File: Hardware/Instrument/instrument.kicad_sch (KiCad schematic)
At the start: 0 parts

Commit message: Added untested op amp circuits for all three devices.
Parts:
- added C3: 1uF, symbol Device:C_Small
- added J1, J3: Esp32 socket, Connector_PinSocket_2.54mm:PinSocket_1x19_P2.54mm_Vertical, symbol Connector:Conn_01x19_Socket
- added MK1: Electret microphone, symbol Device:Microphone
- added R2: 1.5k?, symbol Device:R_Small
- added R7: 100k?, symbol Device:R_Small
- added R8: 500k, symbol Device:R_Small
- added R9: 500k?, symbol Device:R_Small
- added RV2: 1M?, symbol Device:R_Potentiometer_Trim
- added U2: MCP6002-xP, symbol Amplifier_Operational:MCP6002-xP
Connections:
- new net: R8.2, R9.1, U2.3 (+)
- new net: R7.2, RV2.2, RV2.3, U2.2 (-)
- new net: C3.1, MK1.2 (+), R2.2
- new net: C3.2, R7.1
- new net: U2.5 (+), U2.6 (-)
- new net +3.3V: J3.1 (Pin_1), R2.1, R9.2, U2.8 (V+)
- new net +5V: J3.19 (Pin_19)
- new net 0: J1.14 (Pin_14)
- new net 12: J3.13 (Pin_13)
- new net 13: J3.15 (Pin_15)
- new net 14: J3.12 (Pin_12)
- new net 15: J1.16 (Pin_16)
- new net 16: J1.12 (Pin_12)
- new net 17: J1.11 (Pin_11)
- new net 18: J1.9 (Pin_9)
- new net 19: J1.8 (Pin_8)
- new net 2: J1.15 (Pin_15)
- new net 21: J1.6 (Pin_6)
- new net 22: J1.3 (Pin_3)
- new net 23: J1.2 (Pin_2)
- new net 26: J3.10 (Pin_10)
- new net 27: J3.11 (Pin_11)
- new net 32: J3.7 (Pin_7)
- new net 33: J3.8 (Pin_8)
- new net 34: J3.5 (Pin_5)
- new net 35: J3.6 (Pin_6)
- new net 4: J1.13 (Pin_13)
- new net 5: J1.10 (Pin_10)
- new net CLK: J1.19 (Pin_19)
- new net CMD: J3.18 (Pin_18)
- new net D1: J1.17 (Pin_17)
- new net D2: J3.16 (Pin_16)
- new net D3: J3.17 (Pin_17)
- new net D9: J1.18 (Pin_18)
- new net DAC1: J3.9 (Pin_9)
- new net EN: J3.2 (Pin_2)
- new net GND: J1.1 (Pin_1), J1.7 (Pin_7), J3.14 (Pin_14), MK1.1 (-), R8.1, U2.4 (V-)
- new net RX: J1.5 (Pin_5)
- new net TX: J1.4 (Pin_4)
- new net VN: J3.4 (Pin_4)
- new net VP: J3.3 (Pin_3), RV2.1, U2.1
- no-connect marks 0 -> 1
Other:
- note added: "ESP32"

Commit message: added PDF of hardware. Very small (if any) hardware changes.
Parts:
- R7: value 100k? -> 50k?
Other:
- note added: "LP filter?"
- note added: "MULTICOMP PRO ABM-713-RC"
- moved on the sheet: C3, MK1, R2, R7, R8, R9, RV2, U2A

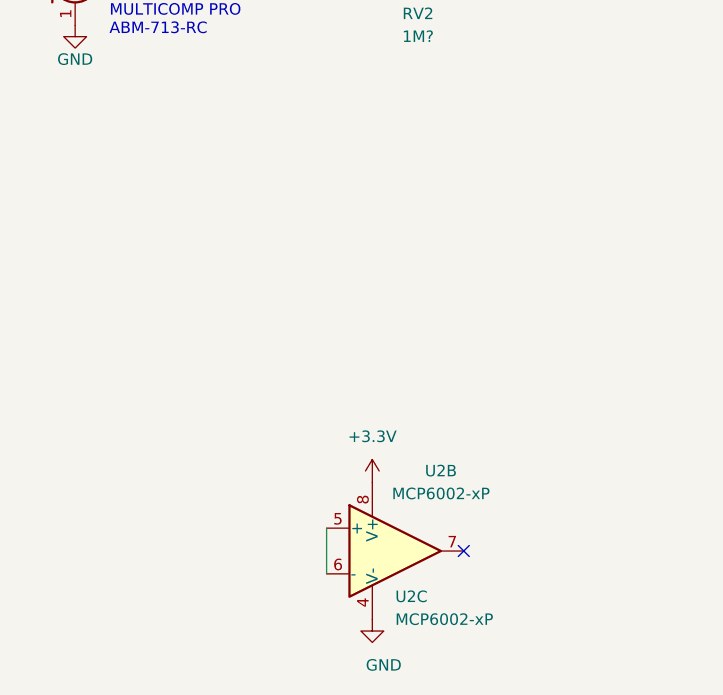
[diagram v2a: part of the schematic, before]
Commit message: Greatly simplified the gateway/speaker module. Added a rectifying circuit and a comparator circuit to the bass drum module. Solidified some component values. Added decoupling capacitors to the schematic.
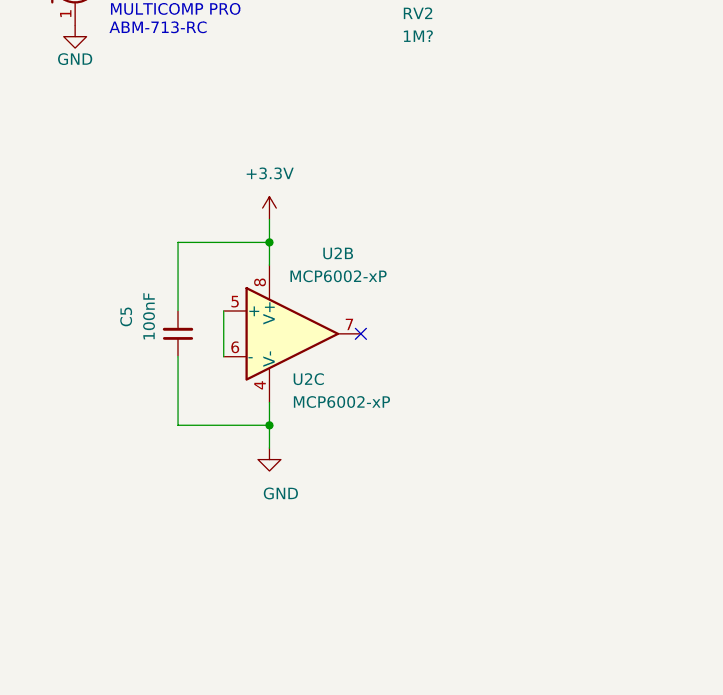
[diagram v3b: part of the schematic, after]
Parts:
- added C5: 100nF, symbol Device:C_Small
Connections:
- net +3.3V: now also C5.2
- net GND: now also C5.1
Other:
- moved on the sheet: U2B, U2C
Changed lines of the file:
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@@
     (company "Studentorchesteret den Ohmske Motstanden")
   )
+  (junction (at 53.34 147.32) (diameter 0) (color 0 0 0 0)
+  )
   (junction (at 80.01 87.63) (diameter 0) (color 0 0 0 0)
   )
@@
   (junction (at 62.23 90.17) (diameter 0) (color 0 0 0 0)
   )
+  (junction (at 53.34 127) (diameter 0) (color 0 0 0 0)
+  )
   (junction (at 62.23 95.25) (diameter 0) (color 0 0 0 0)
   )
-  (no_connect (at 74.93 161.29))
+  (no_connect (at 63.5 137.16))
   (wire (pts (xy 59.69 90.17) (xy 62.23 90.17))
     (stroke (width 0) (type default))
@@
     (stroke (width 0) (type default))
   )
+  (wire (pts (xy 53.34 149.86) (xy 53.34 147.32))
+    (stroke (width 0) (type default))
+  )
   (wire (pts (xy 55.88 66.04) (xy 55.88 68.58))
     (stroke (width 0) (type default))
   )
+  (wire (pts (xy 53.34 124.46) (xy 53.34 127))
+    (stroke (width 0) (type default))
+  )
   (wire (pts (xy 133.35 115.57) (xy 128.27 115.57))
     (stroke (width 0) (type default))
   )
+  (wire (pts (xy 53.34 127) (xy 43.18 127))
+    (stroke (width 0) (type default))
+  )
   (wire (pts (xy 34.29 90.17) (xy 31.75 90.17))
     (stroke (width 0) (type default))
@@
     (stroke (width 0) (type default))
   )
+  (wire (pts (xy 53.34 127) (xy 53.34 129.54))
+    (stroke (width 0) (type default))
+  )
   (wire (pts (xy 31.75 90.17) (xy 31.75 92.71))
     (stroke (width 0) (type default))
@@
     (stroke (width 0) (type default))
   )
+  (wire (pts (xy 53.34 147.32) (xy 53.34 144.78))
+    (stroke (width 0) (type default))
+  )
   (wire (pts (xy 69.85 99.06) (xy 62.23 99.06))
     (stroke (width 0) (type default))
   )
+  (wire (pts (xy 43.18 127) (xy 43.18 134.62))
+    (stroke (width 0) (type default))
+  )
   (wire (pts (xy 55.88 68.58) (xy 62.23 68.58))
     (stroke (width 0) (type default))
@@
     (stroke (width 0) (type default))
   )
-  (wire (pts (xy 59.69 158.75) (xy 59.69 163.83))
+  (wire (pts (xy 48.26 134.62) (xy 48.26 139.7))
     (stroke (width 0) (type default))
   )
@@
     (stroke (width 0) (type default))
   )
+  (wire (pts (xy 43.18 147.32) (xy 53.34 147.32))
+    (stroke (width 0) (type default))
+  )
   (wire (pts (xy 80.01 95.25) (xy 80.01 87.63))
     (stroke (width 0) (type default))
@@
     (stroke (width 0) (type default))
   )
+  (wire (pts (xy 43.18 139.7) (xy 43.18 147.32))
+    (stroke (width 0) (type default))
+  )
   (rectangle (start 170.18 133.35) (end 107.95 71.12)
     (stroke (width 0) (type default))
@@
     (effects (font (size 1.27 1.27)) (justify left bottom))
   )
+  (symbol (lib_id "Device:C_Small") (at 43.18 137.16 180) (unit 1)
+    (in_bom yes) (on_board yes) (dnp no)
+    (property "Reference" "C5" (at 37.465 135.255 90)
+      (effects (font (size 1.27 1.27)))
+    )
+    (property "Value" "100nF" (at 40.005 135.255 90)
+      (effects (font (size 1.27 1.27)))
+    )
+    (property "Footprint" "" (at 43.18 137.16 0)
+      (effects (font (size 1.27 1.27)) hide)
+    )
+    (property "Datasheet" "~" (at 43.18 137.16 0)
+      (effects (font (size 1.27 1.27)) hide)
+    )
+    (pin "1")
+    (pin "2")
+    (instances
+      (project "Stink-overview"
+        (path "/cabf8207-5290-464d-a5db-d31c713ce03c/9cff79f6-1e38-4fd8-974e-e06f4e0c362c"
+          (reference "C5") (unit 1)
+        )
+      )
+    )
+  )
   (symbol (lib_id "power:PWR_FLAG") (at 137.16 82.55 270) (unit 1)
     (in_bom yes) (on_board yes) (dnp no)
@@
     )
   )
-  (symbol (lib_id "power:+3.3V") (at 64.77 153.67 0) (unit 1)
+  (symbol (lib_id "power:+3.3V") (at 53.34 124.46 0) (unit 1)
     (in_bom yes) (on_board yes) (dnp no) (fields_autoplaced)
-    (property "Reference" "#PWR03" (at 64.77 157.48 0)
+    (property "Reference" "#PWR03" (at 53.34 128.27 0)
       (effects (font (size 1.27 1.27)) hide)
     )
-    (property "Value" "+3.3V" (at 64.77 148.59 0)
+    (property "Value" "+3.3V" (at 53.34 119.38 0)
       (effects (font (size 1.27 1.27)))
     )
-    (property "Footprint" "" (at 64.77 153.67 0)
+    (property "Footprint" "" (at 53.34 124.46 0)
       (effects (font (size 1.27 1.27)) hide)
     )
-    (property "Datasheet" "" (at 64.77 153.67 0)
+    (property "Datasheet" "" (at 53.34 124.46 0)
       (effects (font (size 1.27 1.27)) hide)
     )
@@
     )
   )
-  (symbol (lib_id "Amplifier_Operational:MCP6002-xP") (at 67.31 161.29 0) (unit 3)
+  (symbol (lib_id "Amplifier_Operational:MCP6002-xP") (at 55.88 137.16 0) (unit 3)
     (in_bom yes) (on_board yes) (dnp no)
-    (property "Reference" "U2" (at 67.31 166.37 0)
+    (property "Reference" "U2" (at 55.88 142.24 0)
       (effects (font (size 1.27 1.27)) (justify left))
     )
-    (property "Value" "MCP6002-xP" (at 67.31 168.91 0)
+    (property "Value" "MCP6002-xP" (at 55.88 144.78 0)
       (effects (font (size 1.27 1.27)) (justify left))
     )
-    (property "Footprint" "" (at 67.31 161.29 0)
+    (property "Footprint" "" (at 55.88 137.16 0)
       (effects (font (size 1.27 1.27)) hide)
     )
-    (property "Datasheet" "http://ww1.microchip.com/downloads/en/DeviceDoc/21733j.pdf" (at 67.31 161.29 0)
+    (property "Datasheet" "http://ww1.microchip.com/downloads/en/DeviceDoc/21733j.pdf" (at 55.88 137.16 0)
       (effects (font (size 1.27 1.27)) hide)
     )
@@
     )
   )
-  (symbol (lib_id "power:GND") (at 64.77 168.91 0) (unit 1)
+  (symbol (lib_id "power:GND") (at 53.34 149.86 0) (unit 1)
     (in_bom yes) (on_board yes) (dnp no)
-    (property "Reference" "#PWR02" (at 64.77 175.26 0)
+    (property "Reference" "#PWR02" (at 53.34 156.21 0)
       (effects (font (size 1.27 1.27)) hide)
     )
-    (property "Value" "GND" (at 66.04 173.99 0)
+    (property "Value" "GND" (at 54.61 154.94 0)
       (effects (font (size 1.27 1.27)))
     )
-    (property "Footprint" "" (at 64.77 168.91 0)
+    (property "Footprint" "" (at 53.34 149.86 0)
       (effects (font (size 1.27 1.27)) hide)
     )
-    (property "Datasheet" "" (at 64.77 168.91 0)
+    (property "Datasheet" "" (at 53.34 149.86 0)
       (effects (font (size 1.27 1.27)) hide)
     )
@@
     )
   )
-  (symbol (lib_id "Amplifier_Operational:MCP6002-xP") (at 67.31 161.29 0) (unit 2)
+  (symbol (lib_id "Amplifier_Operational:MCP6002-xP") (at 55.88 137.16 0) (unit 2)
     (in_bom yes) (on_board yes) (dnp no)
-    (property "Reference" "U2" (at 72.39 152.4 0)
+    (property "Reference" "U2" (at 60.96 128.27 0)
       (effects (font (size 1.27 1.27)))
     )
-    (property "Value" "MCP6002-xP" (at 72.39 154.94 0)
+    (property "Value" "MCP6002-xP" (at 60.96 130.81 0)
       (effects (font (size 1.27 1.27)))
     )
-    (property "Footprint" "" (at 67.31 161.29 0)
+    (property "Footprint" "" (at 55.88 137.16 0)
       (effects (font (size 1.27 1.27)) hide)
     )
-    (property "Datasheet" "http://ww1.microchip.com/downloads/en/DeviceDoc/21733j.pdf" (at 67.31 161.29 0)
+    (property "Datasheet" "http://ww1.microchip.com/downloads/en/DeviceDoc/21733j.pdf" (at 55.88 137.16 0)
       (effects (font (size 1.27 1.27)) hide)
     )
@@
       (effects (font (size 1.27 1.27)) hide)
     )
-    (property "Datasheet" "~" (at 31.75 95.25 90)
+    (property "Datasheet" "https://www.farnell.com/datasheets/2869766.pdf" (at 31.75 95.25 90)
       (effects (font (size 1.27 1.27)) hide)
     )

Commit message: added batteries to the schematic.
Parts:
- added BT1: Battery, symbol Device:Battery
- added SW1: SW_SPST, symbol Switch:SW_SPST
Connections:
- net GND: now also BT1.2 (-)
- net +5V renamed Vin
- net Vin: now also SW1.2 (B)
- new net: BT1.1 (+), SW1.1 (A)
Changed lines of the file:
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@@
   (junction (at 137.16 82.55) (diameter 0) (color 0 0 0 0)
   )
-  (junction (at 132.08 128.27) (diameter 0) (color 0 0 0 0)
-  )
   (junction (at 133.35 115.57) (diameter 0) (color 0 0 0 0)
   )
@@
     (stroke (width 0) (type default))
   )
+  (wire (pts (xy 176.53 107.95) (xy 176.53 110.49))
+    (stroke (width 0) (type default))
+  )
   (wire (pts (xy 34.29 90.17) (xy 31.75 90.17))
     (stroke (width 0) (type default))
@@
     (stroke (width 0) (type default))
   )
-  (wire (pts (xy 132.08 128.27) (xy 128.27 128.27))
-    (stroke (width 0) (type default))
-  )
   (wire (pts (xy 148.59 82.55) (xy 149.86 82.55))
     (stroke (width 0) (type default))
@@
     (stroke (width 0) (type default))
   )
+  (wire (pts (xy 176.53 123.19) (xy 176.53 120.65))
+    (stroke (width 0) (type default))
+  )
   (wire (pts (xy 69.85 99.06) (xy 62.23 99.06))
     (stroke (width 0) (type default))
@@
     (stroke (width 0) (type default))
   )
+  (wire (pts (xy 176.53 95.25) (xy 176.53 97.79))
+    (stroke (width 0) (type default))
+  )
   (wire (pts (xy 55.88 68.58) (xy 62.23 68.58))
     (stroke (width 0) (type default))
@@
     (effects (font (size 1.27 1.27)) (justify right bottom))
   )
+  (label "Vin" (at 128.27 128.27 0) (fields_autoplaced)
+    (effects (font (size 1.27 1.27)) (justify left bottom))
+  )
   (label "19" (at 149.86 100.33 180) (fields_autoplaced)
     (effects (font (size 1.27 1.27)) (justify right bottom))
@@
     (effects (font (size 1.27 1.27)) (justify left bottom))
   )
+  (label "Vin" (at 176.53 95.25 0) (fields_autoplaced)
+    (effects (font (size 1.27 1.27)) (justify left bottom))
+  )
   (label "TX" (at 149.86 90.17 180) (fields_autoplaced)
     (effects (font (size 1.27 1.27)) (justify right bottom))
@@
     )
   )
-  (symbol (lib_id "power:+5V") (at 132.08 128.27 180) (unit 1)
+  (symbol (lib_id "power:+3.3V") (at 55.88 60.96 0) (unit 1)
     (in_bom yes) (on_board yes) (dnp no) (fields_autoplaced)
-    (property "Reference" "#PWR01" (at 132.08 124.46 0)
+    (property "Reference" "#PWR03" (at 55.88 64.77 0)
       (effects (font (size 1.27 1.27)) hide)
     )
-    (property "Value" "+5V" (at 132.08 132.08 0)
+    (property "Value" "+3.3V" (at 55.88 55.88 0)
       (effects (font (size 1.27 1.27)))
     )
-    (property "Footprint" "" (at 132.08 128.27 0)
+    (property "Footprint" "" (at 55.88 60.96 0)
       (effects (font (size 1.27 1.27)) hide)
     )
-    (property "Datasheet" "" (at 132.08 128.27 0)
+    (property "Datasheet" "" (at 55.88 60.96 0)
       (effects (font (size 1.27 1.27)) hide)
     )
@@
       (project "Aktuator-ESP"
         (path "/355dd754-d0d4-46b9-8352-e30cc265914f"
-          (reference "#PWR01") (unit 1)
+          (reference "#PWR03") (unit 1)
         )
       )
       (project "Stink-overview"
         (path "/cabf8207-5290-464d-a5db-d31c713ce03c/9cff79f6-1e38-4fd8-974e-e06f4e0c362c"
-          (reference "#PWR032") (unit 1)
+          (reference "#PWR033") (unit 1)
         )
         (path "/cabf8207-5290-464d-a5db-d31c713ce03c/8d7bbeab-1973-44b8-aed2-4e4d1a62bc12"
-          (reference "#PWR026") (unit 1)
+          (reference "#PWR024") (unit 1)
         )
       )
     )
   )
-  (symbol (lib_id "power:+3.3V") (at 55.88 60.96 0) (unit 1)
-    (in_bom yes) (on_board yes) (dnp no) (fields_autoplaced)
-    (property "Reference" "#PWR03" (at 55.88 64.77 0)
+  (symbol (lib_id "power:GND") (at 176.53 123.19 0) (unit 1)
+    (in_bom yes) (on_board yes) (dnp no)
+    (property "Reference" "#PWR02" (at 176.53 129.54 0)
       (effects (font (size 1.27 1.27)) hide)
     )
-    (property "Value" "+3.3V" (at 55.88 55.88 0)
+    (property "Value" "GND" (at 177.8 128.27 0)
       (effects (font (size 1.27 1.27)))
     )
-    (property "Footprint" "" (at 55.88 60.96 0)
+    (property "Footprint" "" (at 176.53 123.19 0)
       (effects (font (size 1.27 1.27)) hide)
     )
-    (property "Datasheet" "" (at 55.88 60.96 0)
+    (property "Datasheet" "" (at 176.53 123.19 0)
       (effects (font (size 1.27 1.27)) hide)
     )
@@
       (project "Aktuator-ESP"
         (path "/355dd754-d0d4-46b9-8352-e30cc265914f"
-          (reference "#PWR03") (unit 1)
+          (reference "#PWR02") (unit 1)
         )
       )
       (project "Stink-overview"
         (path "/cabf8207-5290-464d-a5db-d31c713ce03c/9cff79f6-1e38-4fd8-974e-e06f4e0c362c"
-          (reference "#PWR033") (unit 1)
+          (reference "#PWR040") (unit 1)
         )
         (path "/cabf8207-5290-464d-a5db-d31c713ce03c/8d7bbeab-1973-44b8-aed2-4e4d1a62bc12"
-          (reference "#PWR024") (unit 1)
+          (reference "#PWR025") (unit 1)
+        )
+        (path "/cabf8207-5290-464d-a5db-d31c713ce03c/c3cf50cb-25cf-454a-ad63-d86ff0651171"
+          (reference "#PWR035") (unit 1)
         )
       )
@@
     )
   )
-  (symbol (lib_id "power:PWR_FLAG") (at 132.08 128.27 270) (unit 1)
-    (in_bom yes) (on_board yes) (dnp no)
-    (property "Reference" "#FLG02" (at 133.985 128.27 0)
-      (effects (font (size 1.27 1.27)) hide)
-    )
-    (property "Value" "PWR_FLAG" (at 133.35 130.81 90)
-      (effects (font (size 1.27 1.27)) (justify left))
-    )
-    (property "Footprint" "" (at 132.08 128.27 0)
-      (effects (font (size 1.27 1.27)) hide)
-    )
-    (property "Datasheet" "~" (at 132.08 128.27 0)
-      (effects (font (size 1.27 1.27)) hide)
-    )
-    (pin "1")
-    (instances
-      (project "Aktuator-ESP"
-        (path "/355dd754-d0d4-46b9-8352-e30cc265914f"
-          (reference "#FLG02") (unit 1)
-        )
-      )
-      (project "Stink-overview"
-        (path "/cabf8207-5290-464d-a5db-d31c713ce03c/9cff79f6-1e38-4fd8-974e-e06f4e0c362c"
-          (reference "#FLG015") (unit 1)
-        )
-        (path "/cabf8207-5290-464d-a5db-d31c713ce03c/8d7bbeab-1973-44b8-aed2-4e4d1a62bc12"
-          (reference "#FLG012") (unit 1)
-        )
-      )
-    )
-  )
   (symbol (lib_id "Amplifier_Operational:MCP6002-xP") (at 69.85 87.63 0) (unit 1)
     (in_bom yes) (on_board yes) (dnp no) (fields_autoplaced)
@@
     )
   )
+  (symbol (lib_id "Device:Battery") (at 176.53 115.57 0) (unit 1)
+    (in_bom yes) (on_board yes) (dnp no) (fields_autoplaced)
+    (property "Reference" "BT1" (at 180.34 113.7285 0)
+      (effects (font (size 1.27 1.27)) (justify left))
+    )
+    (property "Value" "Battery" (at 180.34 116.2685 0)
+      (effects (font (size 1.27 1.27)) (justify left))
+    )
+    (property "Footprint" "" (at 176.53 114.046 90)
+      (effects (font (size 1.27 1.27)) hide)
+    )
+    (property "Datasheet" "~" (at 176.53 114.046 90)
+      (effects (font (size 1.27 1.27)) hide)
+    )
+    (pin "1")
+    (pin "2")
+    (instances
+      (project "Stink-overview"
+        (path "/cabf8207-5290-464d-a5db-d31c713ce03c/c3cf50cb-25cf-454a-ad63-d86ff0651171"
+          (reference "BT1") (unit 1)
+        )
+        (path "/cabf8207-5290-464d-a5db-d31c713ce03c/9cff79f6-1e38-4fd8-974e-e06f4e0c362c"
+          (reference "BT2") (unit 1)
+        )
+      )
+    )
+  )
   (symbol (lib_id "power:+3.3V") (at 31.75 82.55 0) (unit 1)
     (in_bom yes) (on_board yes) (dnp no)
@@
         )
       )
+    )
+  )
+  (symbol (lib_id "Switch:SW_SPST") (at 176.53 102.87 90) (unit 1)
+    (in_bom yes) (on_board yes) (dnp no) (fields_autoplaced)
+    (property "Reference" "SW1" (at 177.8 101.6 90)
+      (effects (font (size 1.27 1.27)) (justify right))
+    )
+    (property "Value" "SW_SPST" (at 177.8 104.14 90)
+      (effects (font (size 1.27 1.27)) (justify right))
+    )
+    (property "Footprint" "" (at 176.53 102.87 0)
+      (effects (font (size 1.27 1.27)) hide)
+    )
+    (property "Datasheet" "~" (at 176.53 102.87 0)
+      (effects (font (size 1.27 1.27)) hide)
+    )
+    (pin "1")
+    (pin "2")
+    (instances
+      (project "Stink-overview"
+        (path "/cabf8207-5290-464d-a5db-d31c713ce03c/c3cf50cb-25cf-454a-ad63-d86ff0651171"
+          (reference "SW1") (unit 1)
+        )
+        (path "/cabf8207-5290-464d-a5db-d31c713ce03c/9cff79f6-1e38-4fd8-974e-e06f4e0c362c"
+          (reference "SW2") (unit 1)
+        )
+      )
